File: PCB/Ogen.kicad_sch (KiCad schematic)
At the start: 17 parts, among them J1 Input, U1 PMW3360DM-T2QU, U2 TLV70019, U3 TXS0102DCU, U4 TXS0102DCU, U5 TXS0102DCU

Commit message: V1.0 Lite initial commit.
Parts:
- removed C1: 4.7uF, Capacitor_SMD:C_0603_1608Metric, symbol Device:C_Small
- removed C2: 100nF, Capacitor_SMD:C_0603_1608Metric, symbol Device:C_Small
- removed C3, C4: 1uF, Capacitor_SMD:C_0603_1608Metric, symbol Device:C_Small
- removed R1, R2: 10k, Resistor_SMD:R_0603_1608Metric, symbol Device:R_Small
- removed R3: 39R, Resistor_SMD:R_0603_1608Metric, symbol Device:R_Small
- removed U1: PMW3360DM-T2QU, Ogen:IC_PMW3360DM-T2QU, symbol Ogen:PMW3360DM-T2QU
- removed U2: TLV70019, Package_TO_SOT_SMD:SOT-23-5, symbol Regulator_Linear:TLV70019_SOT23-5
- removed U3, U4, U5: TXS0102DCU, Package_SO:VSSOP-8_2.3x2mm_P0.5mm, symbol Logic_LevelTranslator:TXS0102DCU
- added C21 (x2): 1u, Capacitor_SMD:C_0402_1005Metric, symbol Device:C_Small
- added C93: 4u7, Capacitor_SMD:C_0603_1608Metric, symbol Device:C_Small
- added C94: 100n, Capacitor_SMD:C_0402_1005Metric, symbol Device:C_Small
- added R10, R14, R27: 10k, Resistor_SMD:R_0402_1005Metric, symbol Device:R_Small
- added R11: 39, Resistor_SMD:R_0402_1005Metric, symbol Device:R_Small
- added R28: 15k, Resistor_SMD:R_0402_1005Metric, symbol Device:R_Small
- added U4: PMW3360DM-T2QU, Ogen:IC_PMW3360DM-T2QU, symbol Ogen:PMW3360DM-T2QU
- added U6: AP2127K-ADJ, Package_TO_SOT_SMD:SOT-23-5, symbol Regulator_Linear:AP2127K-ADJ
- A1: footprint Ogen:Ariamelon_Logo -> Ogen:Ariamelon_Logo-CU; symbol Mechanical:MountingHole -> Mechanical:Fiducial
- J1: footprint Connector_PinHeader_2.54mm:PinHeader_1x08_P2.54mm_Vertical -> Ogen:PinHeader_1x08_P2.54mm_Vertical
- JP1: value Jumper -> MISO_Pullup; now left out of the parts list
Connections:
- net MISO-H is gone; now on net MISO: J1.2 (Pin_2)
- net MOSI-H is gone; now on net MOSI: J1.3 (Pin_3)
- net GND: now also C21.2, C21.2, C93.2, C94.1, R27.2, U4.8 (GND), U6.2 (GND)
- net MISO: now also U4.12 (MISO)
- net MOSI: now also U4.11 (MOSI)
- net at JP1.1 (A): now also R14.1
- net MOT-H renamed MOTION
- net MOTION: now also U4.9 (MOTION)
- net NRESET-H renamed ~{RST}
- net ~{RST}: now also R10.1, U4.7 (NRESET)
- net SCLK-H renamed SCK
- net SCK: now also U4.10 (SCLK)
- net SS-H renamed CS
- net CS: now also U4.13 (NCS)
- net VCC renamed +3V3
- net +3V3: now also C21.1, R10.2, R14.2, U4.5 (VDDIO), U6.1 (VIN), U6.3 (EN)
- new net: C93.1, C94.2, U4.3 (VDDPIX)
- new net: R27.1, R28.2, U6.4 (ADJ)
- new net: R11.1, U4.15 (LED_P)
- new net: U4.1 (NC), U4.14 (NC), U4.16 (NC), U4.2 (NC), U4.6 (NC)
- new net +2V: C21.1, R11.2, R28.1, U4.4 (VDD), U6.5 (VOUT)
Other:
- moved on the sheet: H1, H2

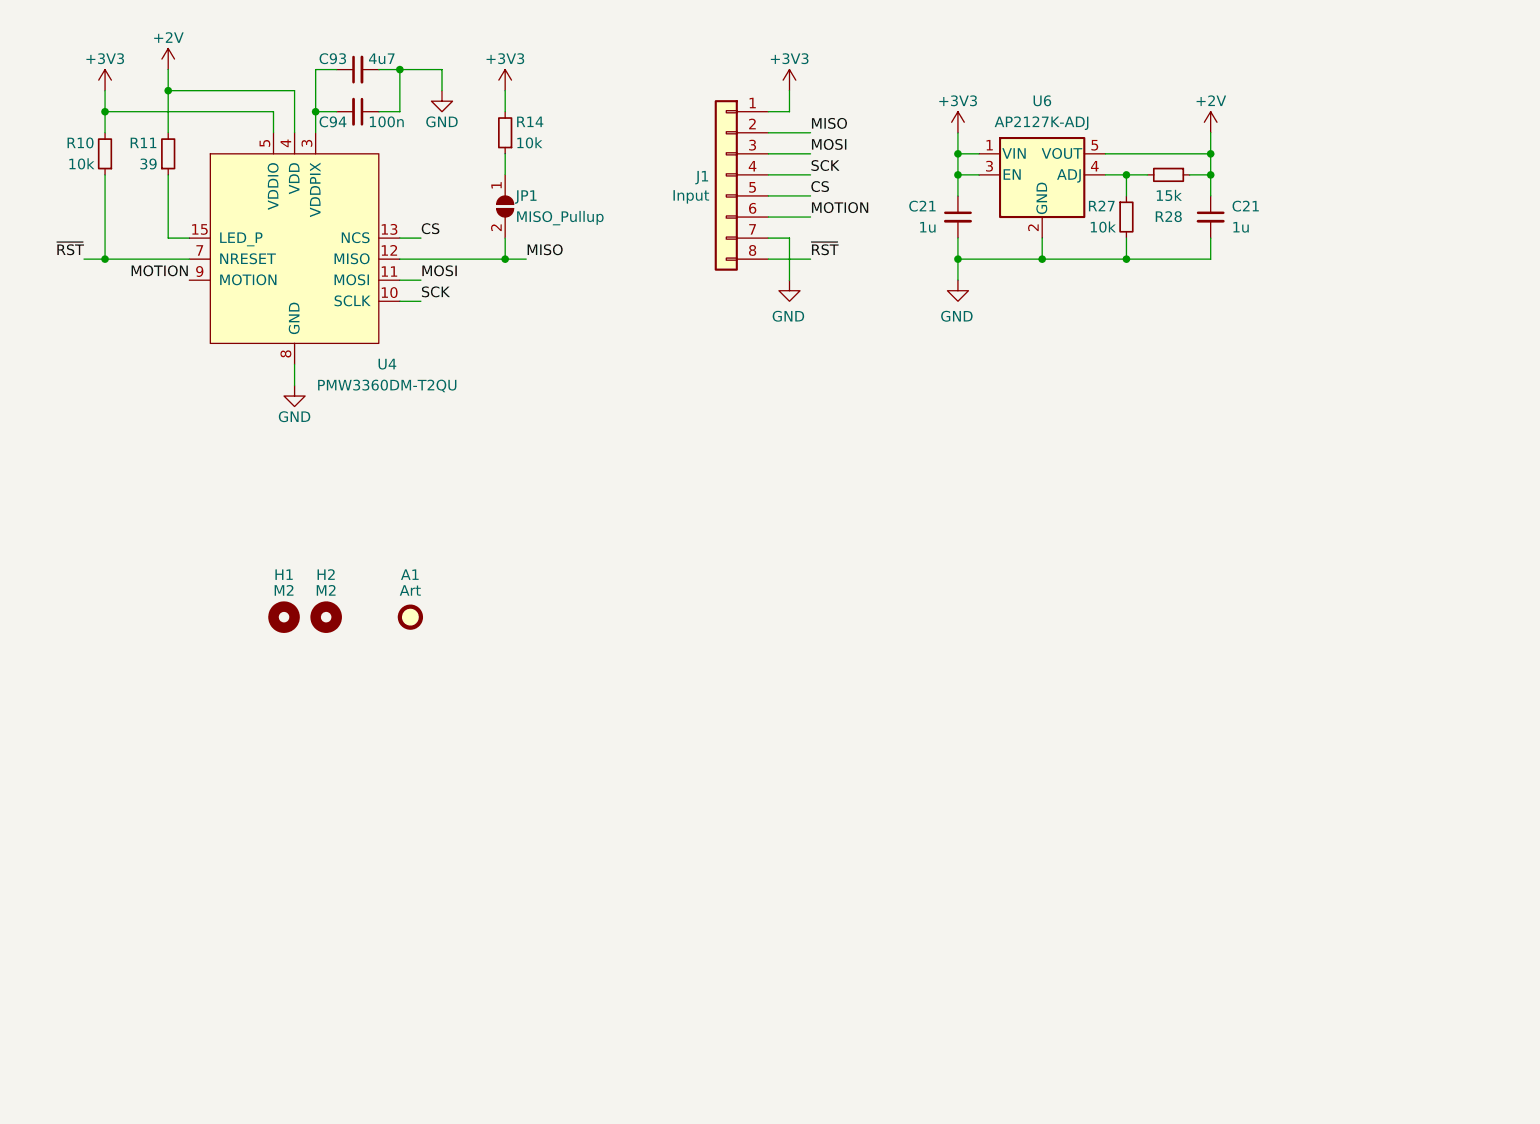
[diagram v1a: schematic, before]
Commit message: 04/08/2023 update
Updated to V1.1. Changed capacitors and resistors to 0603. Stitched ground planes together. Removed MISO pullup jumper (MISO is pulled up by default now). Added metadata to schematic and PCB file. Changed location of production files for easier access.
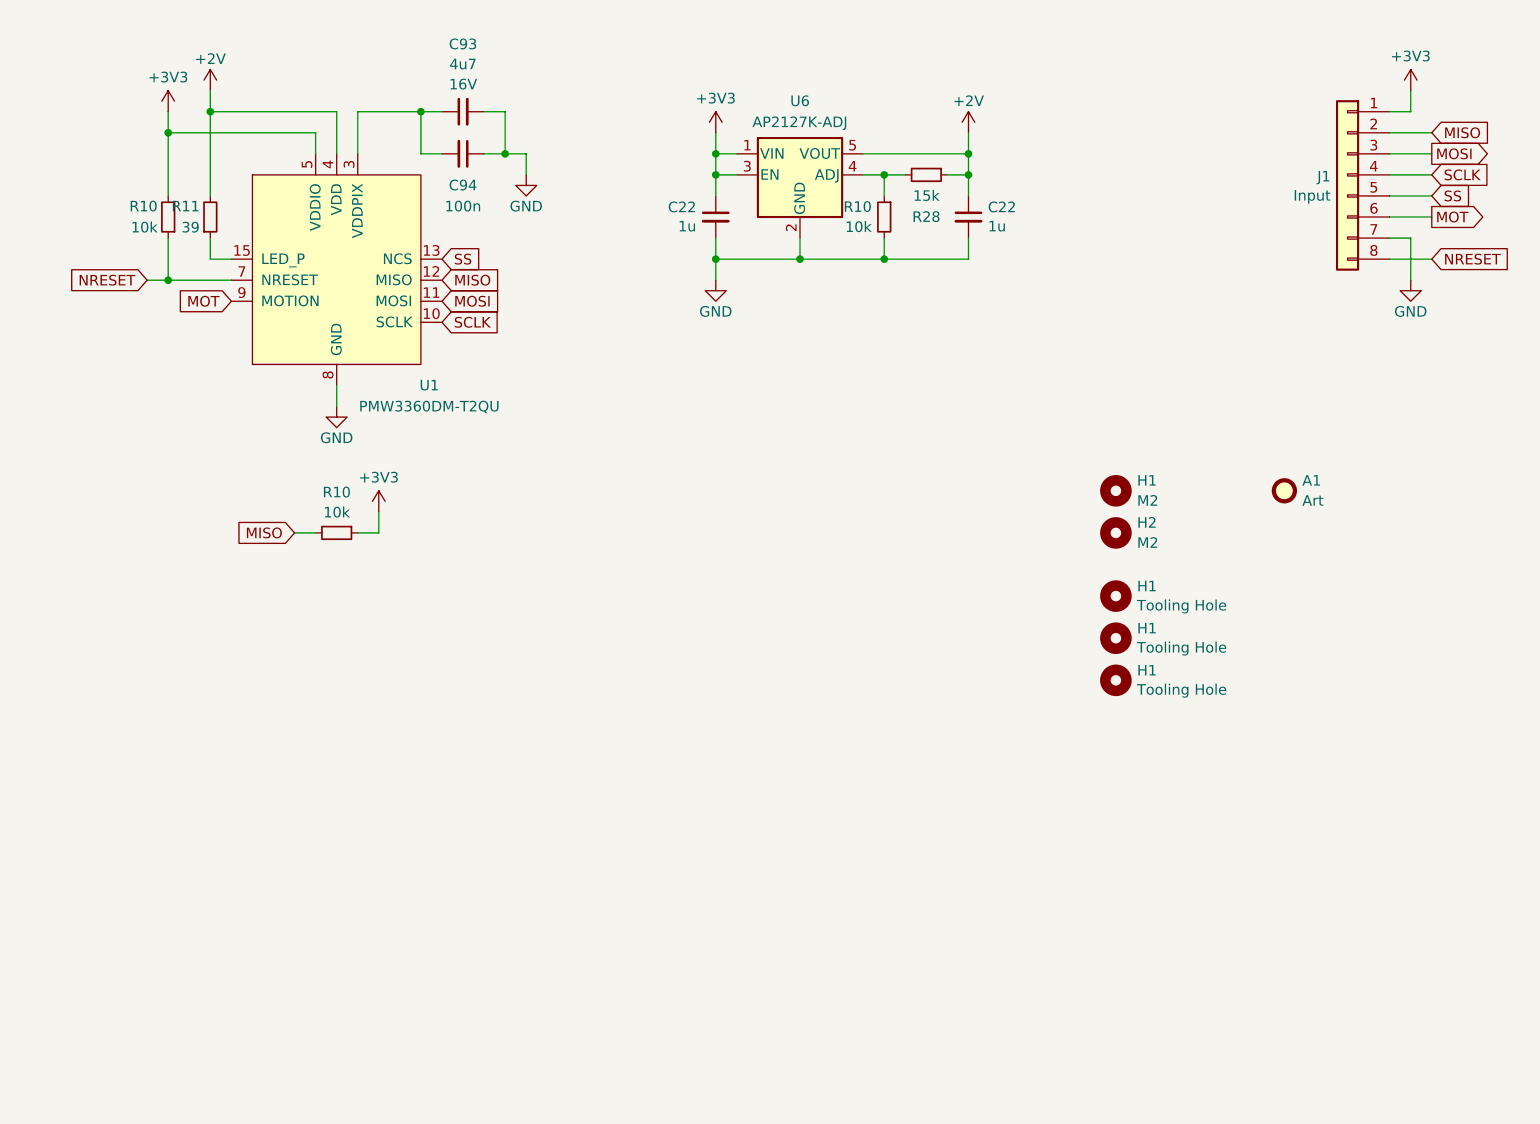
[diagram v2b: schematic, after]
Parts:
- removed C21 (x2): 1u, Capacitor_SMD:C_0402_1005Metric, symbol Device:C_Small
- removed JP1: MISO_Pullup, Jumper:SolderJumper-2_P1.3mm_Open_Pad1.0x1.5mm, symbol Jumper:SolderJumper_2_Open
- removed R10, R14, R27: 10k, Resistor_SMD:R_0402_1005Metric, symbol Device:R_Small
- removed U4: PMW3360DM-T2QU, Ogen:IC_PMW3360DM-T2QU, symbol Ogen:PMW3360DM-T2QU
- added C22 (x2): 1u, Capacitor_SMD:C_0603_1608Metric, symbol Device:C_Small
- added H1 (x3): Tooling Hole, Ogen:JLC Tooling Hole, symbol Mechanical:MountingHole
- added R10 (x3): 10k, Resistor_SMD:R_0603_1608Metric, symbol Device:R_Small
- added U1: PMW3360DM-T2QU, Ogen:IC_PMW3360DM-T2QU, symbol Ogen:PMW3360DM-T2QU
- A1, H1, H2: now left out of the parts list
- C93: Voltage (none) -> 16V
- C94: footprint Capacitor_SMD:C_0402_1005Metric -> Capacitor_SMD:C_0603_1608Metric; LCSC C1525 -> C14663
- J1: footprint Ogen:PinHeader_1x08_P2.54mm_Vertical -> Connector_PinHeader_2.54mm:PinHeader_1x08_P2.54mm_Vertical; now left out of the parts list
- R11: footprint Resistor_SMD:R_0402_1005Metric -> Resistor_SMD:R_0603_1608Metric; LCSC C25164 -> C25236
- R28: footprint Resistor_SMD:R_0402_1005Metric -> Resistor_SMD:R_0603_1608Metric; LCSC C25756 -> C22809
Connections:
- net +2V: now also C22.1, U1.4 (VDD)
- net +3V3: now also C22.1, R10.1, R10.2, U1.5 (VDDIO)
- net GND: now also C22.2, C22.2, R10.2, U1.8 (GND)
- net MISO: now also R10.2, U1.12 (MISO)
- net MOSI: now also U1.11 (MOSI)
- net at C93.1, C94.2: now also U1.3 (VDDPIX)
- net at R28.2, U6.4 (ADJ): now also R10.1
- net at R11.1: now also U1.15 (LED_P)
- net CS renamed SS
- net SS: now also U1.13 (NCS)
- net MOTION renamed MOT
- net MOT: now also U1.9 (MOTION)
- net SCK renamed SCLK
- net SCLK: now also U1.10 (SCLK)
- net ~{RST} renamed NRESET
- net NRESET: now also R10.1, U1.7 (NRESET)
- new net: U1.1 (NC), U1.14 (NC), U1.16 (NC), U1.2 (NC), U1.6 (NC)
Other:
- company: (none) -> Created by Ariamelon (https://github.com/Ariamelon/Ogen/)
- title: (none) -> Ogen Lite PMW3360 Module
- moved on the sheet: A1, H1, H2

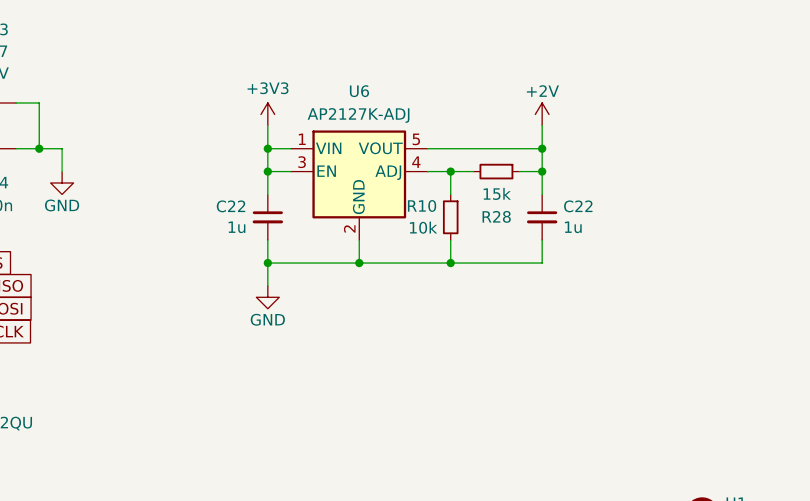
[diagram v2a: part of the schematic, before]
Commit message: 18/09/2023 update
Fixed .gitignore file. Changed LDO capacitors to 4u7 to match the one used in the PMW3360.
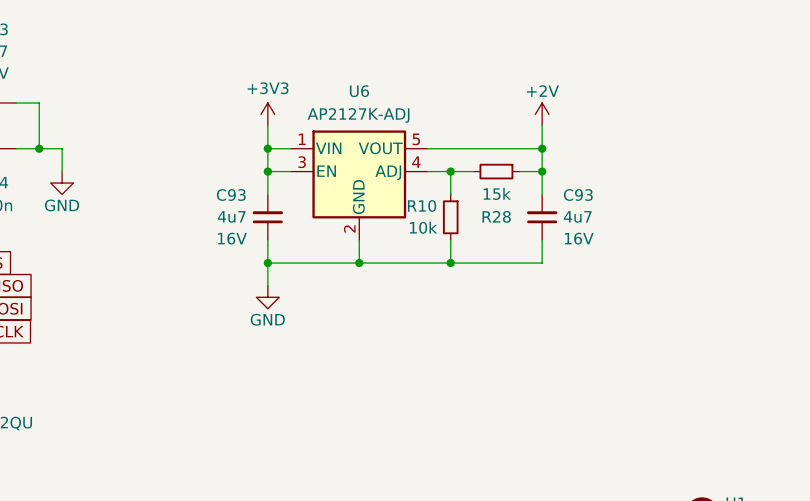
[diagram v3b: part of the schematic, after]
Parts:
- removed C22 (x2): 1u, Capacitor_SMD:C_0603_1608Metric, symbol Device:C_Small
- added C93 (x2): 4u7, Capacitor_SMD:C_0603_1608Metric, symbol Device:C_Small
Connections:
- net +2V: now also C93.2
- net +3V3: now also C93.2
- net GND: now also C93.1, C93.1
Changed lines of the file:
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@@
   (title_block
     (title "Ogen Lite PMW3360 Module")
-    (date "2023-08-04")
-    (rev "V1.1")
+    (date "2023-09-18")
+    (rev "V1.2")
     (company "Created by Ariamelon (https://github.com/Ariamelon/Ogen/)")
     (comment 1 "All capacitors 50V unless otherwise specified.")
@@
     )
   )
+  (symbol (lib_id "Device:C_Small") (at 93.98 38.1 0) (mirror x) (unit 1)
+    (in_bom yes) (on_board yes) (dnp no) (fields_autoplaced)
+    (property "Reference" "C93" (at 91.6559 35.6694 0)
+      (effects (font (size 1.27 1.27)) (justify right))
+    )
+    (property "Value" "4u7" (at 91.6559 38.0936 0)
+      (effects (font (size 1.27 1.27)) (justify right))
+    )
+    (property "Footprint" "Capacitor_SMD:C_0603_1608Metric" (at 93.98 38.1 0)
+      (effects (font (size 1.27 1.27)) hide)
+    )
+    (property "Datasheet" "~" (at 93.98 38.1 0)
+      (effects (font (size 1.27 1.27)) hide)
+    )
+    (property "Description" "0603 capacitor" (at 93.98 38.1 0)
+      (effects (font (size 1.27 1.27)) hide)
+    )
+    (property "LCSC" "C19666" (at 93.98 38.1 0)
+      (effects (font (size 1.27 1.27)) hide)
+    )
+    (property "Voltage" "16V" (at 91.6559 40.5178 0)
+      (effects (font (size 1.27 1.27)) (justify right))
+    )
+    (pin "1")
+    (pin "2")
+    (instances
+      (project "Honeydew"
+        (path "/534caec7-cf60-4f90-b1ed-42c9d445ef0f/3b9d6b66-6ecb-42d2-a8a6-a52a8ef176c3"
+          (reference "C93") (unit 1)
+        )
+      )
+      (project "Ogen"
+        (path "/ee41cb8e-512d-41d2-81e1-3c50fff32aeb"
+          (reference "C3") (unit 1)
+        )
+      )
+    )
+  )
   (symbol (lib_id "Device:R_Small") (at 33.02 38.1 0) (mirror x) (unit 1)
     (in_bom yes) (on_board yes) (dnp no)
@@
         (path "/ee41cb8e-512d-41d2-81e1-3c50fff32aeb"
           (reference "U2") (unit 1)
+        )
+      )
+    )
+  )
+  (symbol (lib_id "Device:C_Small") (at 124.46 38.1 180) (unit 1)
+    (in_bom yes) (on_board yes) (dnp no)
+    (property "Reference" "C93" (at 126.7841 35.6694 0)
+      (effects (font (size 1.27 1.27)) (justify right))
+    )
+    (property "Value" "4u7" (at 126.7841 38.0936 0)
+      (effects (font (size 1.27 1.27)) (justify right))
+    )
+    (property "Footprint" "Capacitor_SMD:C_0603_1608Metric" (at 124.46 38.1 0)
+      (effects (font (size 1.27 1.27)) hide)
+    )
+    (property "Datasheet" "~" (at 124.46 38.1 0)
+      (effects (font (size 1.27 1.27)) hide)
+    )
+    (property "Description" "0603 capacitor" (at 124.46 38.1 0)
+      (effects (font (size 1.27 1.27)) hide)
+    )
+    (property "LCSC" "C19666" (at 124.46 38.1 0)
+      (effects (font (size 1.27 1.27)) hide)
+    )
+    (property "Voltage" "16V" (at 126.7841 40.5178 0)
+      (effects (font (size 1.27 1.27)) (justify right))
+    )
+    (pin "1")
+    (pin "2")
+    (instances
+      (project "Honeydew"
+        (path "/534caec7-cf60-4f90-b1ed-42c9d445ef0f/3b9d6b66-6ecb-42d2-a8a6-a52a8ef176c3"
+          (reference "C93") (unit 1)
+        )
+      )
+      (project "Ogen"
+        (path "/ee41cb8e-512d-41d2-81e1-3c50fff32aeb"
+          (reference "C4") (unit 1)
         )
       )
@@
     )
   )
-  (symbol (lib_id "Device:C_Small") (at 124.46 38.1 0) (unit 1)
-    (in_bom yes) (on_board yes) (dnp no) (fields_autoplaced)
-    (property "Reference" "C22" (at 126.7968 36.9316 0)
-      (effects (font (size 1.27 1.27)) (justify left))
-    )
-    (property "Value" "1u" (at 126.7968 39.243 0)
-      (effects (font (size 1.27 1.27)) (justify left))
-    )
-    (property "Footprint" "Capacitor_SMD:C_0603_1608Metric" (at 124.46 38.1 0)
-      (effects (font (size 1.27 1.27)) hide)
-    )
-    (property "Datasheet" "~" (at 124.46 38.1 0)
-      (effects (font (size 1.27 1.27)) hide)
-    )
-    (property "Description" "0603 capacitor" (at 124.46 38.1 0)
-      (effects (font (size 1.27 1.27)) hide)
-    )
-    (property "LCSC" "C15849" (at 124.46 38.1 0)
-      (effects (font (size 1.27 1.27)) hide)
-    )
-    (pin "1")
-    (pin "2")
-    (instances
-      (project "Honeydew"
-        (path "/534caec7-cf60-4f90-b1ed-42c9d445ef0f/0e23afb1-1d24-49d7-b6b4-dea31b732359"
-          (reference "C22") (unit 1)
-        )
-      )
-      (project "Ogen"
-        (path "/ee41cb8e-512d-41d2-81e1-3c50fff32aeb"
-          (reference "C4") (unit 1)
-        )
-      )
-    )
-  )
   (symbol (lib_id "Mechanical:MountingHole") (at 142.24 93.98 0) (unit 1)
     (in_bom no) (on_board yes) (dnp no)
@@
         )
       )
-    )
-  )
-  (symbol (lib_id "Device:C_Small") (at 93.98 38.1 0) (mirror y) (unit 1)
-    (in_bom yes) (on_board yes) (dnp no)
-    (property "Reference" "C22" (at 91.6432 36.9316 0)
-      (effects (font (size 1.27 1.27)) (justify left))
-    )
-    (property "Value" "1u" (at 91.6432 39.243 0)
-      (effects (font (size 1.27 1.27)) (justify left))
-    )
-    (property "Footprint" "Capacitor_SMD:C_0603_1608Metric" (at 93.98 38.1 0)
-      (effects (font (size 1.27 1.27)) hide)
-    )
-    (property "Datasheet" "~" (at 93.98 38.1 0)
-      (effects (font (size 1.27 1.27)) hide)
-    )
-    (property "Description" "0603 capacitor" (at 93.98 38.1 0)
-      (effects (font (size 1.27 1.27)) hide)
-    )
-    (property "LCSC" "C15849" (at 93.98 38.1 0)
-      (effects (font (size 1.27 1.27)) hide)
-    )
-    (pin "1")
-    (pin "2")
-    (instances
-      (project "Honeydew"
-        (path "/534caec7-cf60-4f90-b1ed-42c9d445ef0f/0e23afb1-1d24-49d7-b6b4-dea31b732359"
-          (reference "C22") (unit 1)
-        )
-      )
-      (project "Ogen"
-        (path "/ee41cb8e-512d-41d2-81e1-3c50fff32aeb"
-          (reference "C3") (unit 1)
-        )
-      )

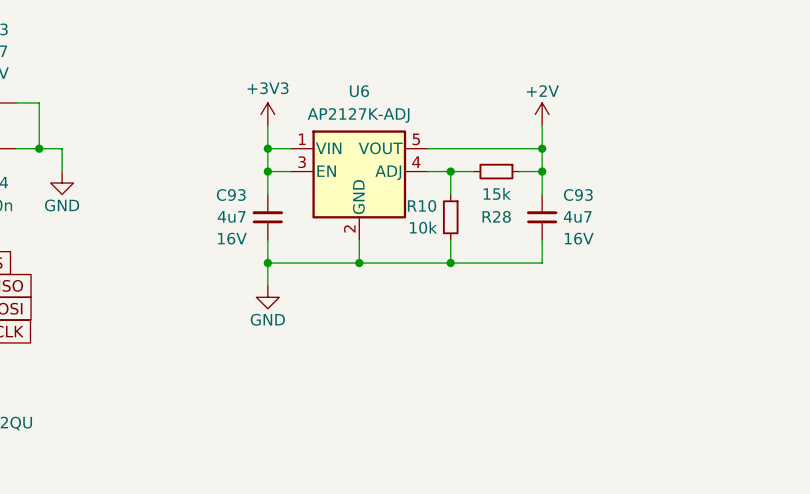
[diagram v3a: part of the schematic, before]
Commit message: V1.3 update
Changed LDO to XC6206P202MR.
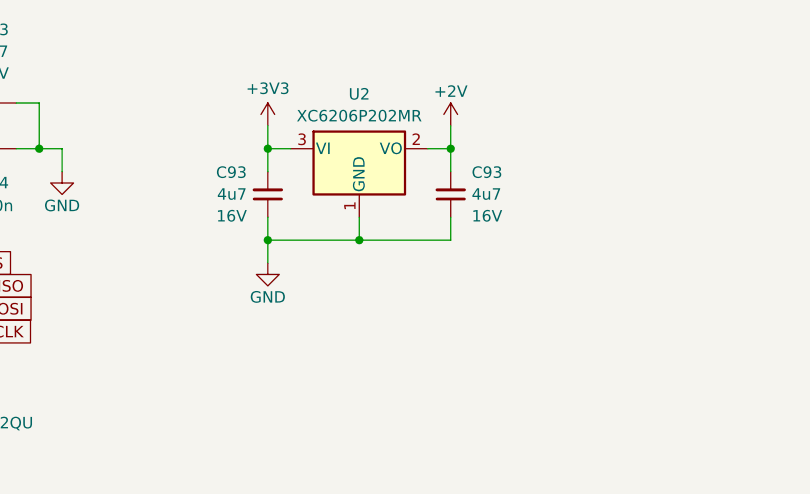
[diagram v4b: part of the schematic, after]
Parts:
- removed R10: 10k, Resistor_SMD:R_0603_1608Metric, symbol Device:R_Small
- removed R28: 15k, Resistor_SMD:R_0603_1608Metric, symbol Device:R_Small
- removed U6: AP2127K-ADJ, Package_TO_SOT_SMD:SOT-23-5, symbol Regulator_Linear:AP2127K-ADJ
- added U2: XC6206P202MR, Ariamelon-Package:SOT-23-3, symbol Regulator_Linear:XC6206PxxxMR
- U1: symbol Ogen:PMW3360DM-T2QU -> Ariamelon-IC:PMW3360DM-T2QU_1
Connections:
- net +2V: now also U2.2 (VO)
- net +3V3: now also U2.3 (VI)
- net GND: now also U2.1 (GND)
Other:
- moved on the sheet: C93
